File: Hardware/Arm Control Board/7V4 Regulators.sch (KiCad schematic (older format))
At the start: 52 parts

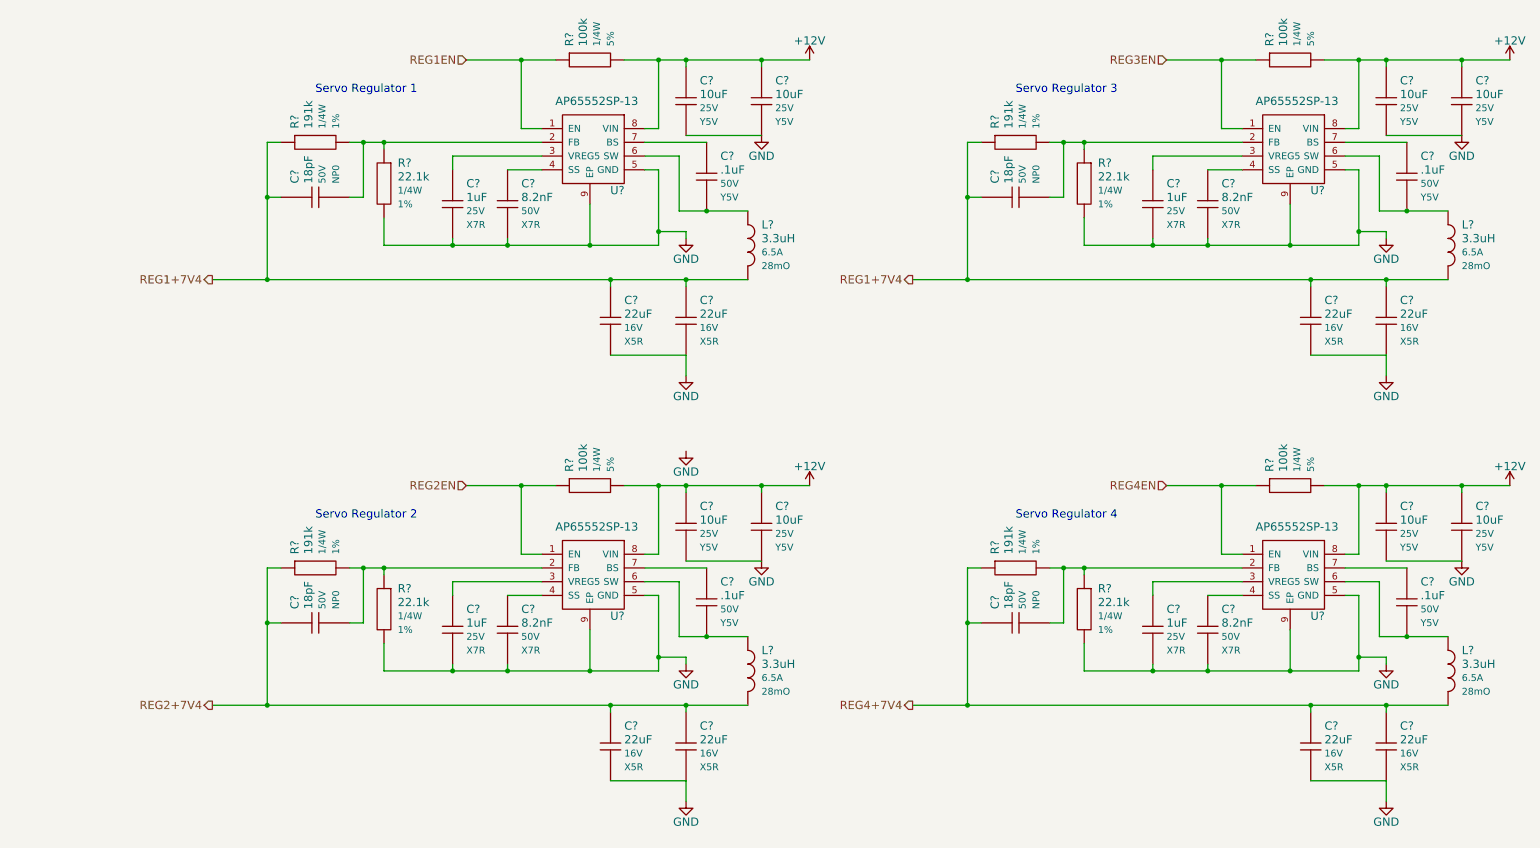
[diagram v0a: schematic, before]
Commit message: More footprints added, components annotated
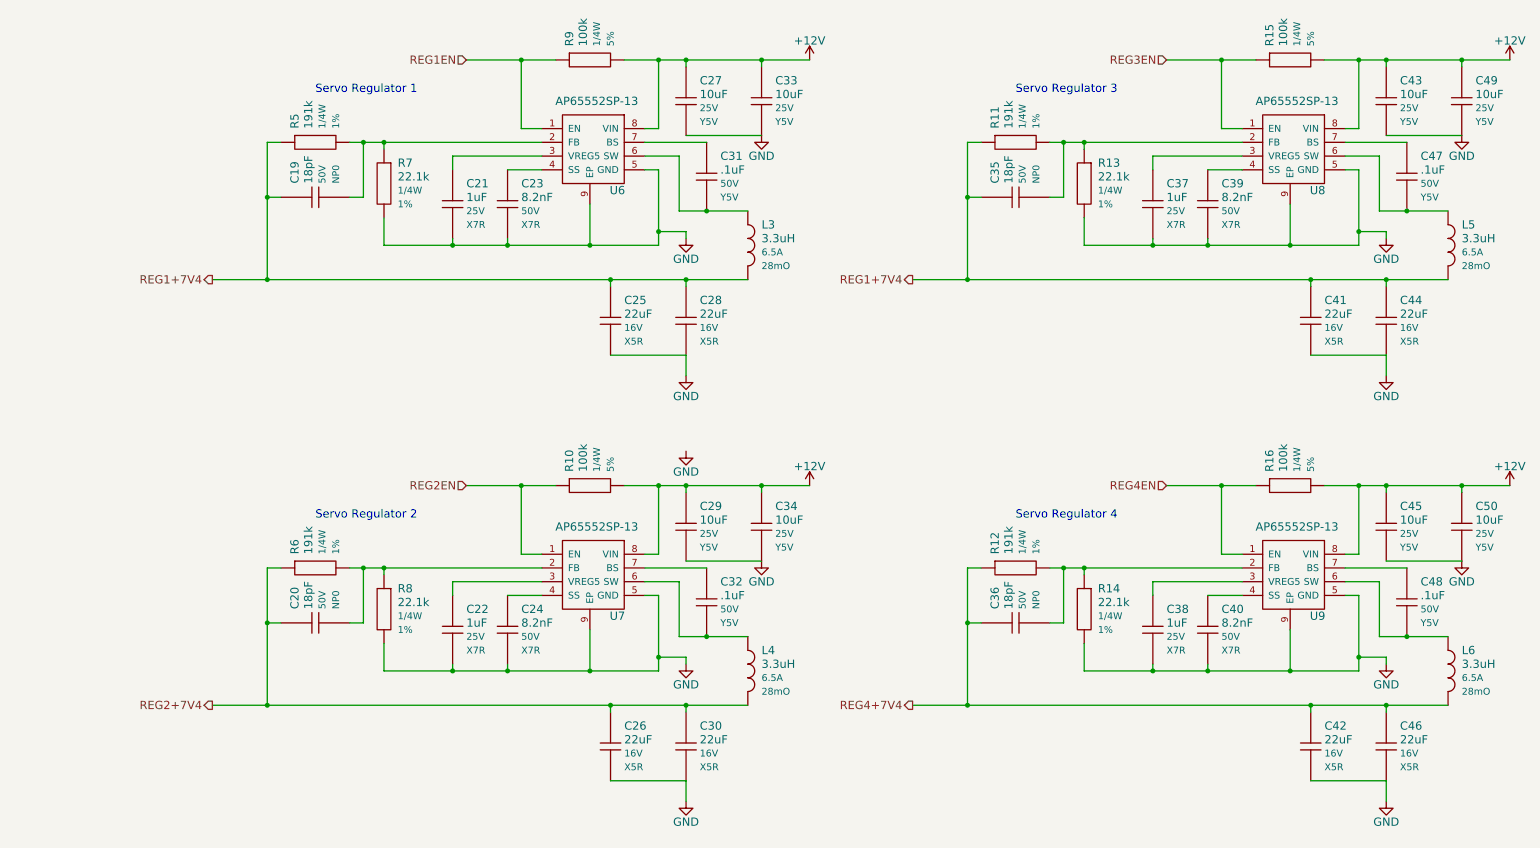
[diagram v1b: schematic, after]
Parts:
- gave numbers to parts that had none: 52

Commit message: Initial PCB layout
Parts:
- U6, U7, U8, U9: footprint (none) -> SMD_Packages:SOIC-8-N-1EP
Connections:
- net REG1+7V4: no longer C35.1, C41.1, C44.1, L5.2, R11.1
- new net REG3+7V4: C35.1, C41.1, C44.1, L5.2, R11.1

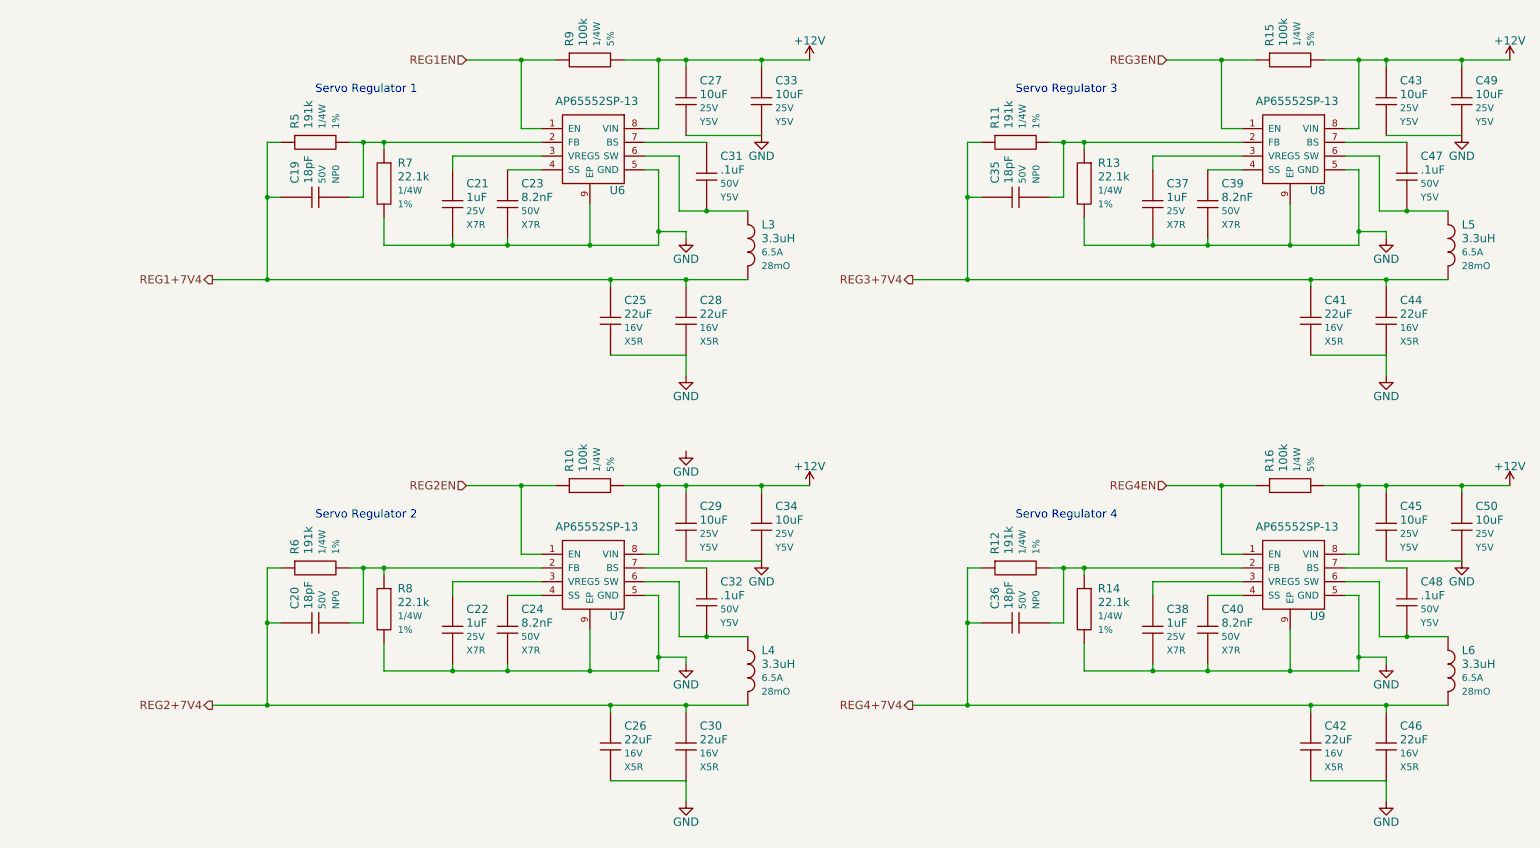
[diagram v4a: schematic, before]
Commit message: Added current sensing to reg1-4, updated STMCube
Only high current servo outputs have current sensing. STMCube was not up
to date with pin assignments. Issues: #18 #15
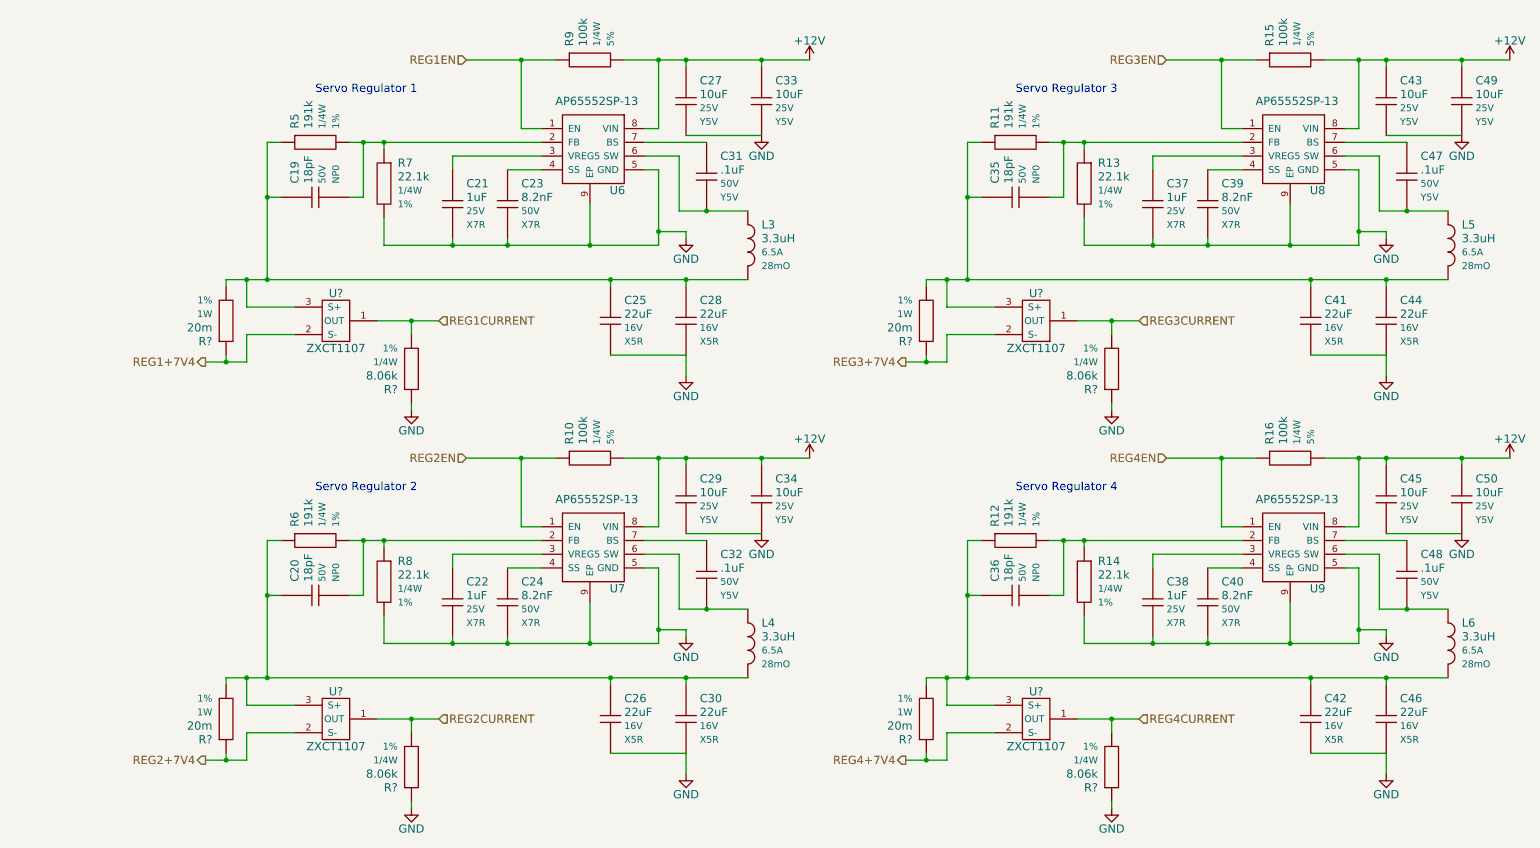
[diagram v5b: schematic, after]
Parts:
- added R? (x4): 20m, Resistors_SMD:R_1206_HandSoldering, symbol Resistor
- added R? (x4): 8.06k, symbol Resistor
- added U? (x4): ZXCT1107, symbol ZXCT1107
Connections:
- net GND: now also R?.1, R?.1, R?.1, R?.1
- net REG1+7V4: now also R?.1, U?.2 (S-); no longer C19.1, C25.1, C28.1, L3.2, R5.1
- net REG2+7V4: now also R?.1, U?.2 (S-); no longer C20.1, C26.1, C30.1, L4.2, R6.1
- net REG3+7V4: now also R?.1, U?.2 (S-); no longer C35.1, C41.1, C44.1, L5.2, R11.1
- net REG4+7V4: now also R?.1, U?.2 (S-); no longer C36.1, C42.1, C46.1, L6.2, R12.1
- new net: C19.1, C25.1, C28.1, L3.2, R5.1, R?.2, U?.3 (S+)
- new net: C20.1, C26.1, C30.1, L4.2, R6.1, R?.2, U?.3 (S+)
- new net: C35.1, C41.1, C44.1, L5.2, R11.1, R?.2, U?.3 (S+)
- new net: C36.1, C42.1, C46.1, L6.2, R12.1, R?.2, U?.3 (S+)
- new net REG1CURRENT: R?.2, U?.1 (OUT)
- new net REG2CURRENT: R?.2, U?.1 (OUT)
- new net REG3CURRENT: R?.2, U?.1 (OUT)
- new net REG4CURRENT: R?.2, U?.1 (OUT)
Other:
- moved on the sheet: C20, C22, C24, C26, C29, C30, C32, C34, C36, C38, C40, C42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

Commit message: Lay out regulators 1-4, update cube for oscillator
Got strangely excited about this commit. Almost called my dad...
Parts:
- R19, R20, R23, R24: renamed from R?; footprint (none) -> Resistors_SMD:R_1206_HandSoldering
- U10, U11, U12, U13: renamed from U?; footprint (none) -> Housings_SOT-23_SOT-143_TSOT-6:SOT23_Transistor_Handsoldering_RevB_14Mar2014
- gave numbers to parts that had none: 4

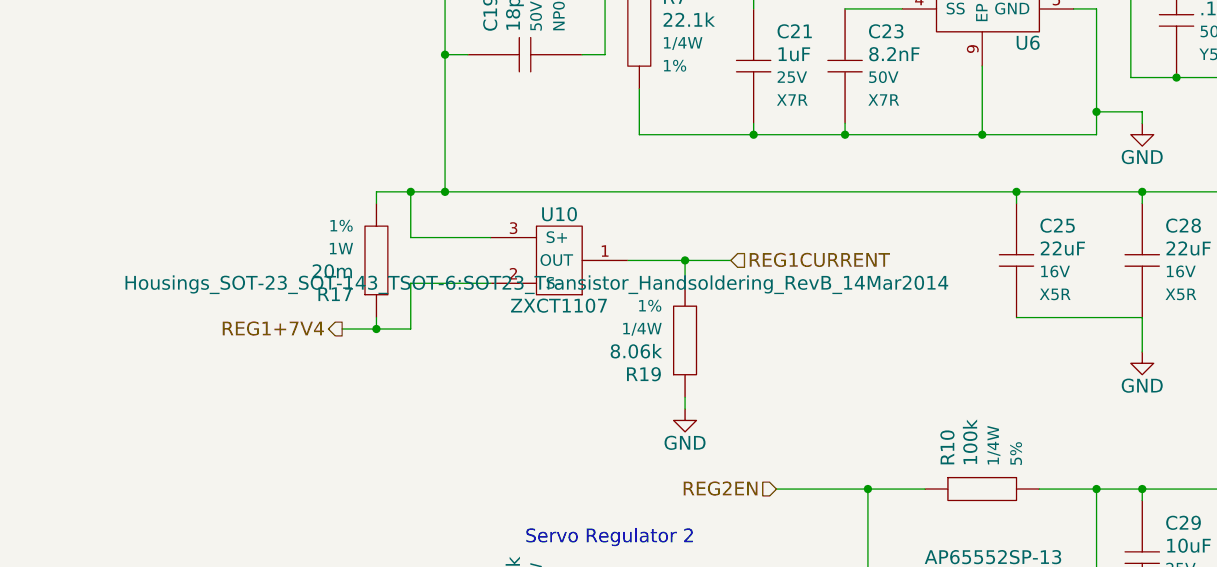
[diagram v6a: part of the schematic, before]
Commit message: Initial layout of Regulator 5 (AOZ)
Followed datasheet recommendations pretty well, probably some room for
improvement
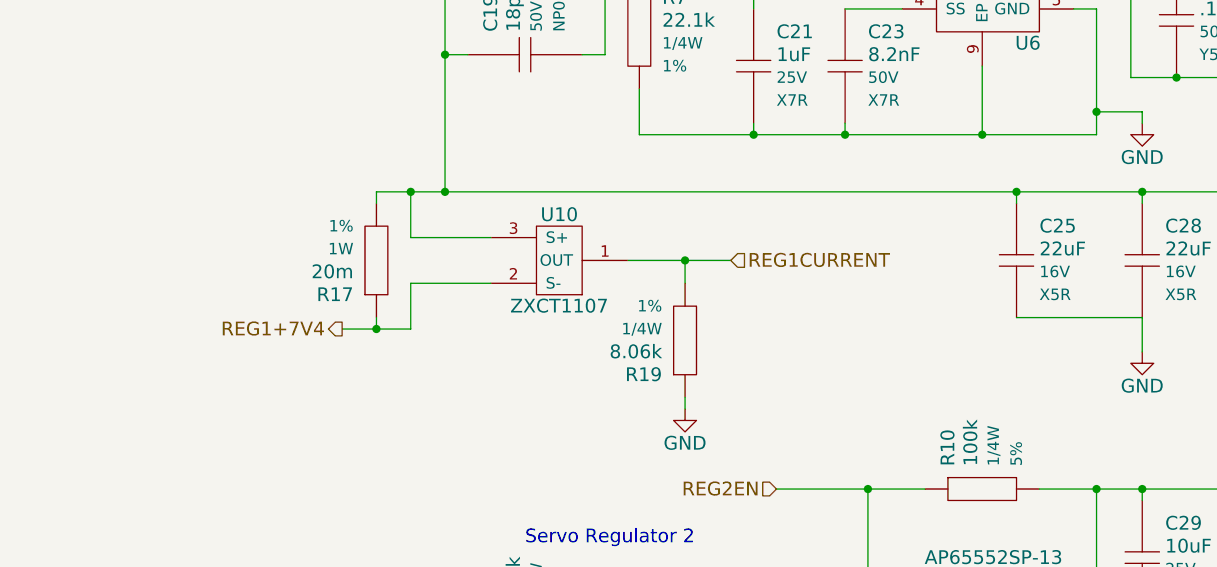
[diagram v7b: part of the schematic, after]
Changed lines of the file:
@@
 F 0 "U10" H 1850 2550 60  0000 C CNN
 F 1 "ZXCT1107" H 1850 2950 60  0000 C CNN
-F 2 "Housings_SOT-23_SOT-143_TSOT-6:SOT23_Transistor_Handsoldering_RevB_14Mar2014" H 1950 2850 60  0000 C CNN
+F 2 "Housings_SOT-23_SOT-143_TSOT-6:SOT23_Transistor_Handsoldering_RevB_14Mar2014" H 1950 2850 60  0001 C CNN
 F 3 "" H 1950 2850 60  0000 C CNN
 	1    1950 2850
